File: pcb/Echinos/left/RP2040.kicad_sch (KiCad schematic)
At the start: 28 parts, among them SW224 Button, SW225 Button, SW226 Button, SW227 Button, U200 W25Q128JVP, U201 RP2040, Y200 Crystal_GND24

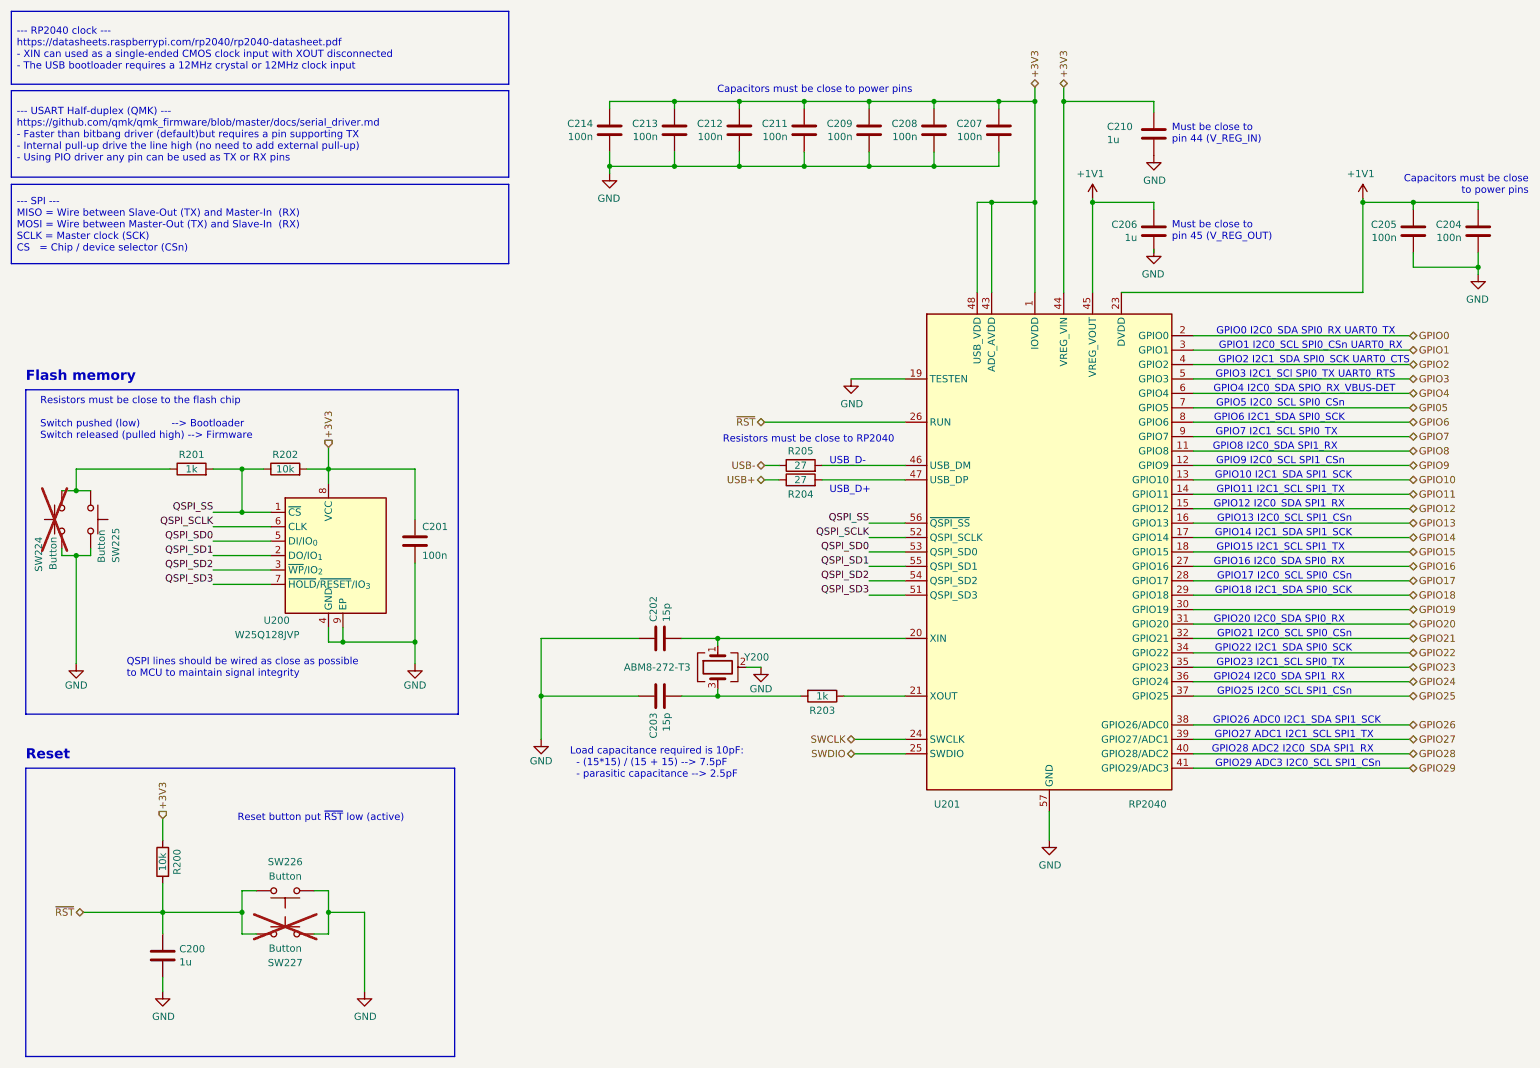
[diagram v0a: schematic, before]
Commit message: 💥 [PCB] - Split schematic for left and right halves.   - Required to create a common PCB to lower the manufacturing cost
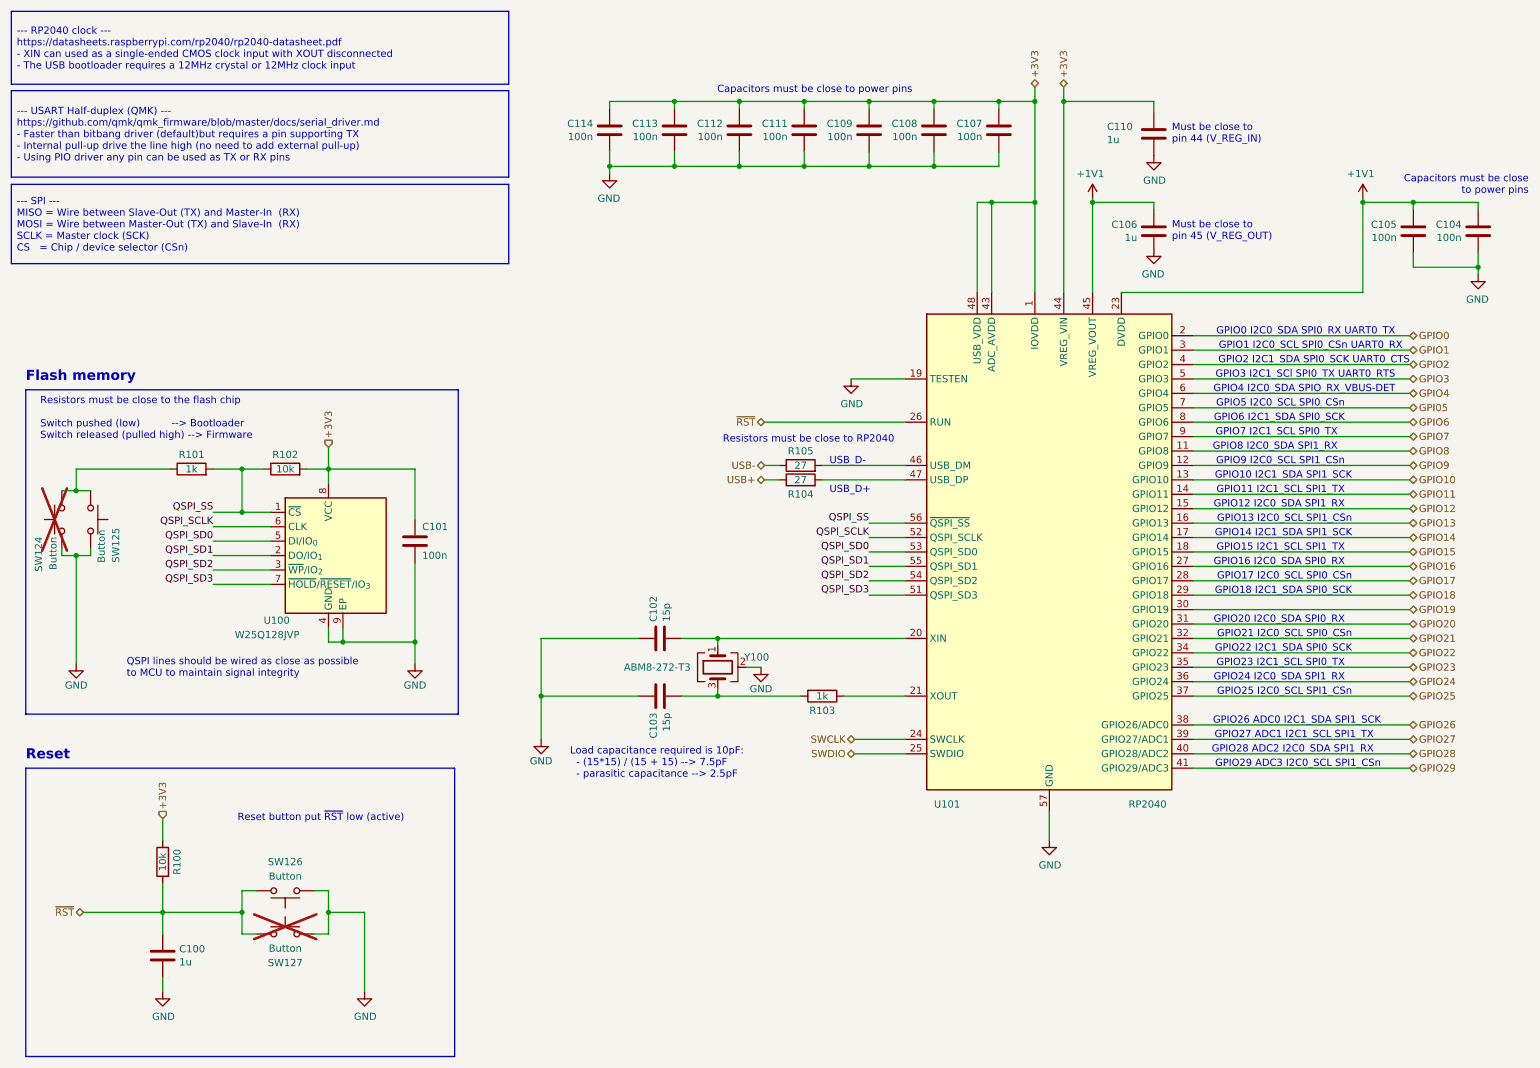
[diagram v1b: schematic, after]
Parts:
- renumbered C200 to C100, C201 to C101, C202 to C102, C203 to C103, C204 to C104, C205 to C105, C206 to C106, C207 to C107, C208 to C108, C209 to C109, C210 to C110, C211 to C111, C212 to C112, C213 to C113, C214 to C114, R200 to R100, R201 to R101, R202 to R102, R203 to R103, R204 to R104, R205 to R105, SW224 to SW124, SW225 to SW125, SW226 to SW126, SW227 to SW127, U200 to U100, U201 to U101, Y200 to Y100

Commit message: 💥 [PCB] - Group left and right on the same PCB.   - Schematics are different for each side   - Split trace naming to avoid mixing right and left   - Add mouse bite between both halves to make manufacturing easier (new footprint)
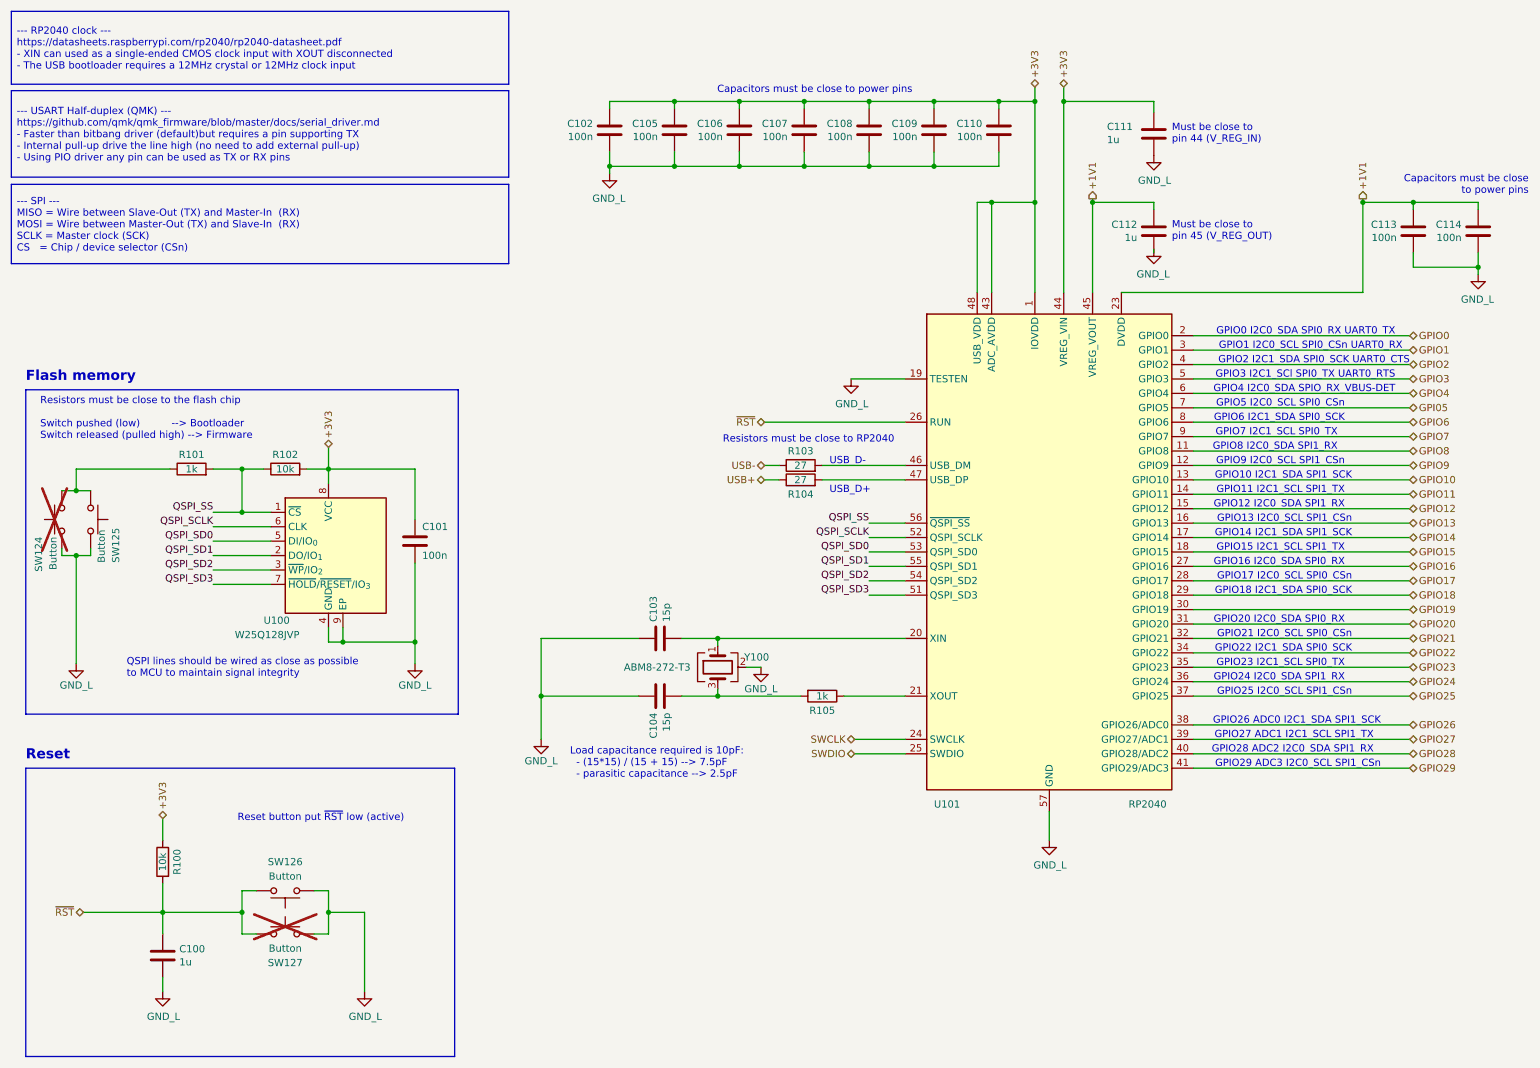
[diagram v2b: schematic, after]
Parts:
- renumbered C114 to C102, C102 to C103, C103 to C104, C113 to C105, C112 to C106, C111 to C107, C109 to C108, C108 to C109, C107 to C110, C110 to C111, C106 to C112, C105 to C113, C104 to C114, R105 to R103, R103 to R105
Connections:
- net GND renamed GND_L
